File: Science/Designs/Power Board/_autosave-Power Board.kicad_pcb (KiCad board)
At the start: 2 copper layers, 114.3 x 90.2 mm, 25 parts, among them P1 PWR_IN, P2 MOTOR_PWR_OUT, P3 MAIN_PWR_OUT, P4 I2C, P5 MOTOR_SW, P6 REG_12V, P7 REG_5V, U1 INA219, U2 INA219, U3 INA219

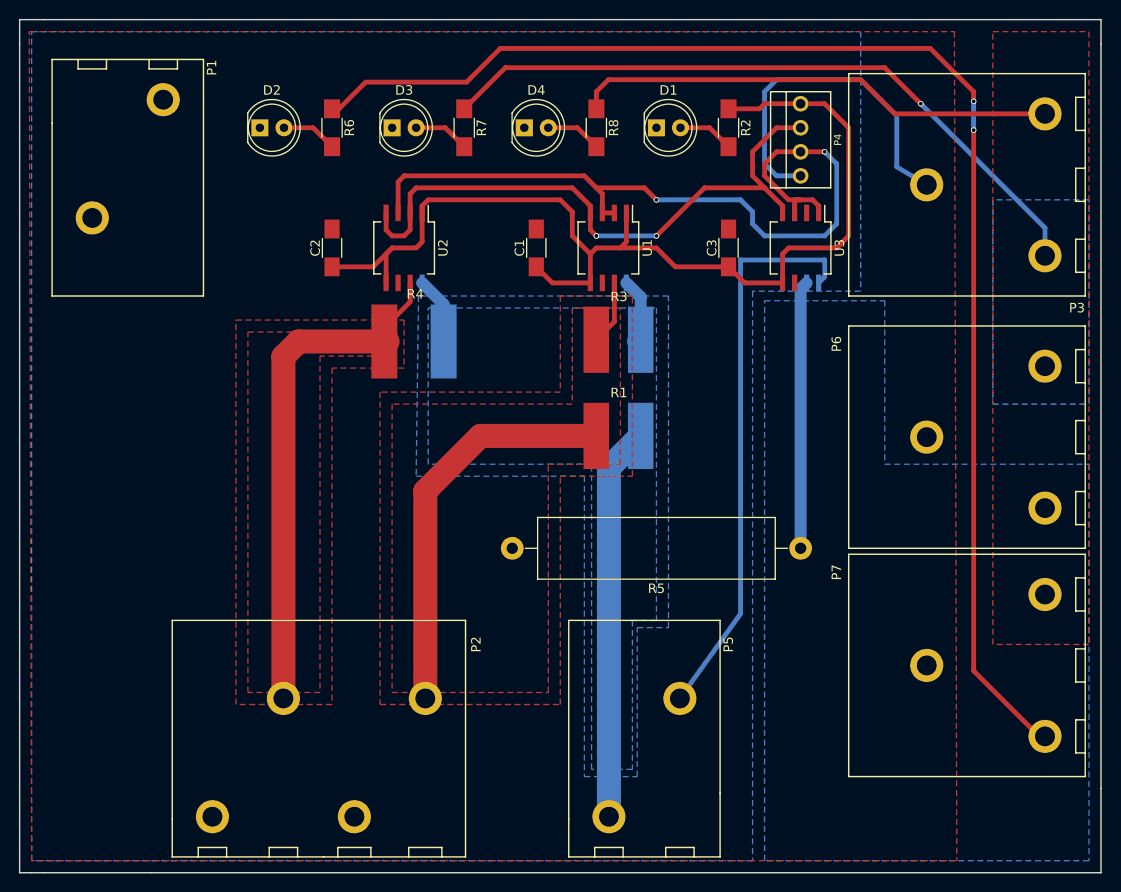
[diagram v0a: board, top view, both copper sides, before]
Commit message: Edited silkscreen
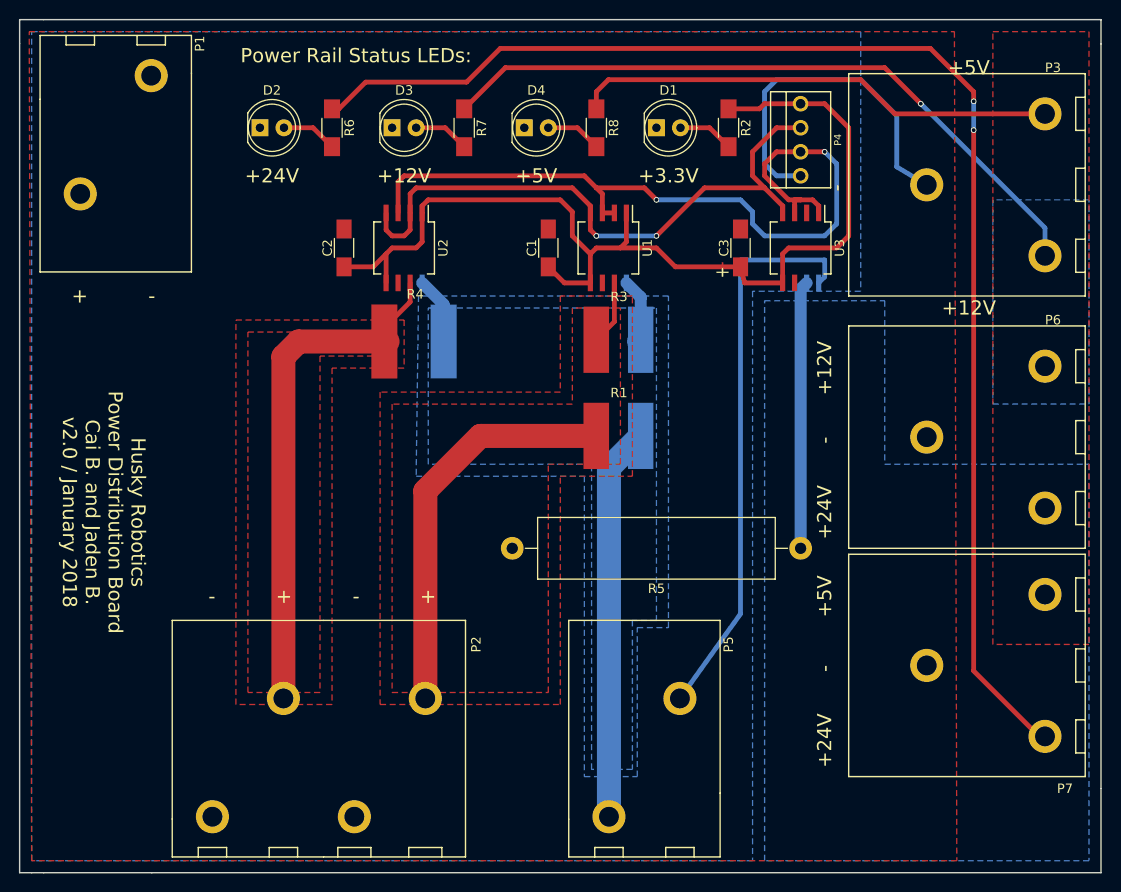
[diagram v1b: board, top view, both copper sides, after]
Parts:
- moved P1 2.84 mm to (83.8, 54.6)
- moved C3 1.27 mm to (149.9, 52.1)
- moved C2 1.27 mm to (108.0, 52.1)
- moved C1 1.27 mm to (129.5, 52.1)
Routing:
- net +3V3: track 113.4 -> 110.0 mm
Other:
- board text added: "+"
- board text added: "+12V"
- board text added: "+24V"
- board text added: "+3.3V"
- board text added: "+5V"
- board text added: "-"
- board text added: "Husky Robotics Power Distribution Board Cai B. and Jaden B. v2.0 / January 2018"
- board text added: "Power Rail Status LEDs:"
